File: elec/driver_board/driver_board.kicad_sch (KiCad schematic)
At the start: 0 parts

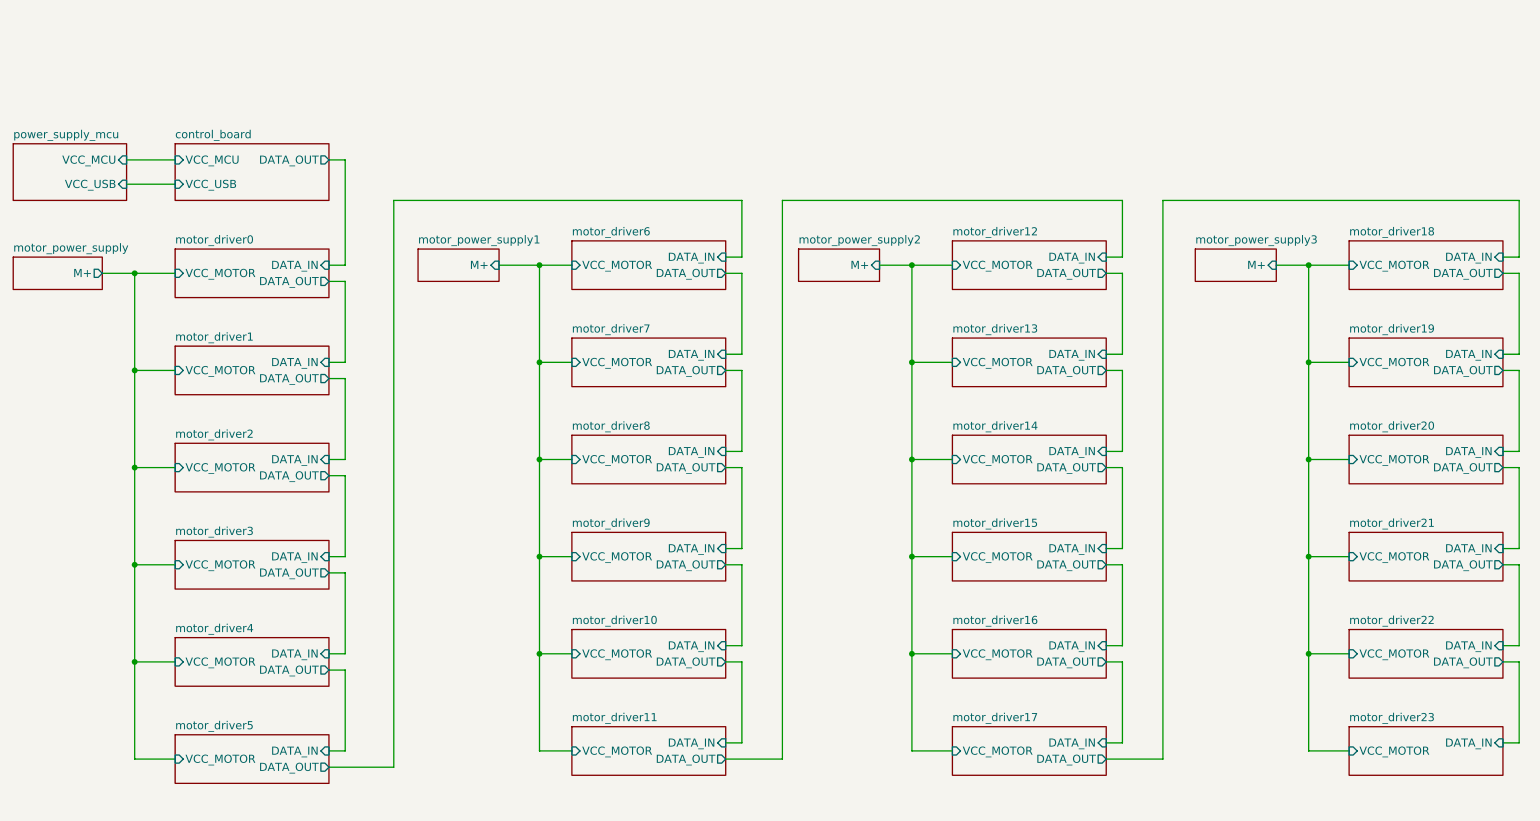
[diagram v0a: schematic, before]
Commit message: [elec] New design with BKA30D-R5
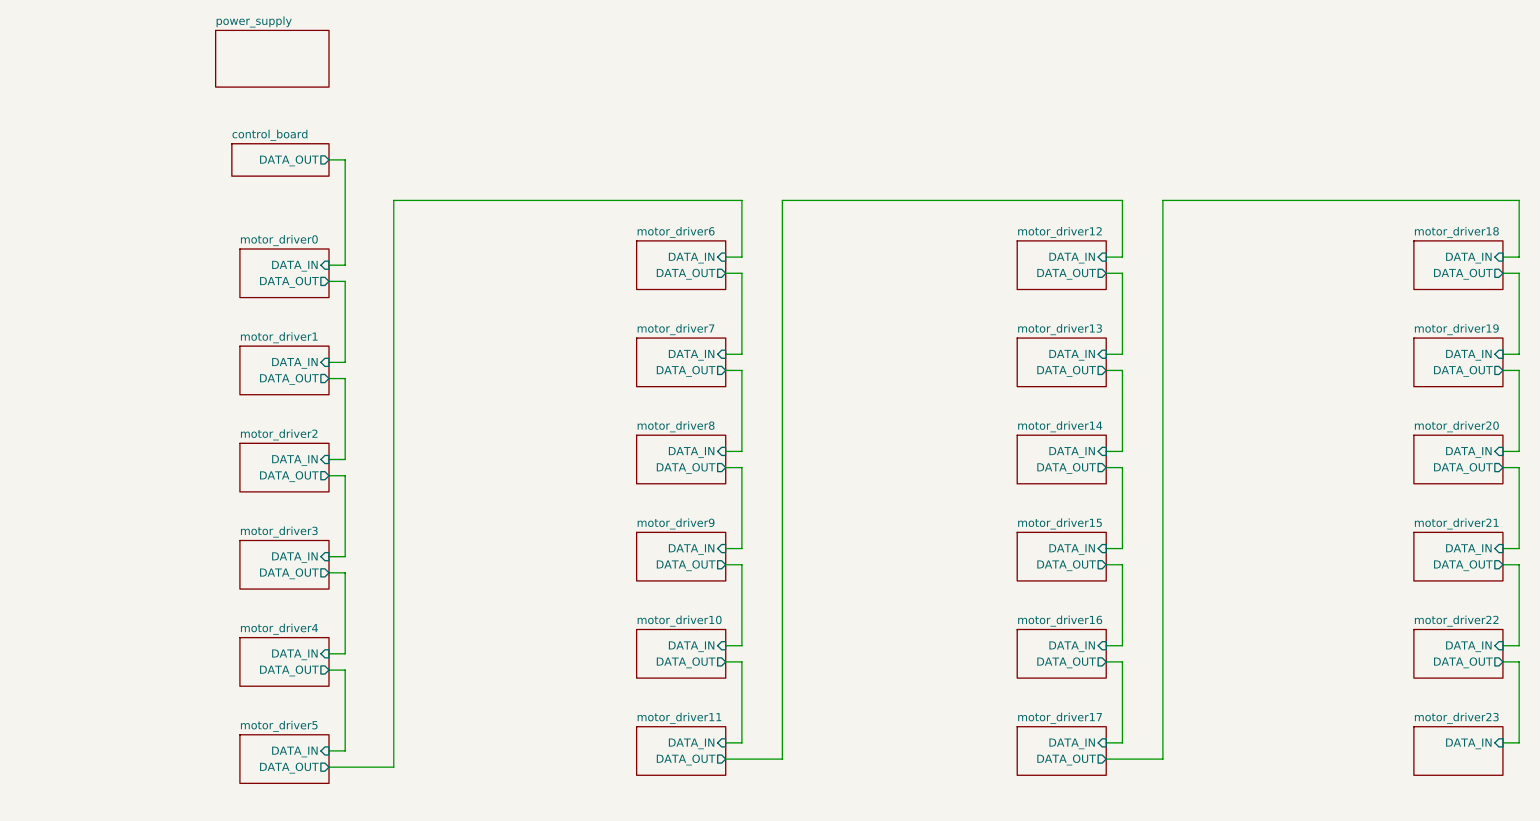
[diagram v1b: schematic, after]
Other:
- sheet power_supply_mcu renamed power_supply
- removed sheet motor_power_supply
- removed sheet motor_power_supply1
- removed sheet motor_power_supply2
- removed sheet motor_power_supply3
- sheet control_board ports: added none; removed VCC_MCU, VCC_USB
- sheet motor_driver0 ports: added none; removed VCC_MOTOR
- sheet motor_driver1 ports: added none; removed VCC_MOTOR
- sheet motor_driver10 ports: added none; removed VCC_MOTOR
- sheet motor_driver11 ports: added none; removed VCC_MOTOR
- sheet motor_driver12 ports: added none; removed VCC_MOTOR
- sheet motor_driver13 ports: added none; removed VCC_MOTOR
- sheet motor_driver14 ports: added none; removed VCC_MOTOR
- sheet motor_driver15 ports: added none; removed VCC_MOTOR
- sheet motor_driver16 ports: added none; removed VCC_MOTOR
- sheet motor_driver17 ports: added none; removed VCC_MOTOR
- sheet motor_driver18 ports: added none; removed VCC_MOTOR
- sheet motor_driver19 ports: added none; removed VCC_MOTOR
- sheet motor_driver2 ports: added none; removed VCC_MOTOR
- sheet motor_driver20 ports: added none; removed VCC_MOTOR
- sheet motor_driver21 ports: added none; removed VCC_MOTOR
- sheet motor_driver22 ports: added none; removed VCC_MOTOR
- sheet motor_driver23 ports: added none; removed VCC_MOTOR
- sheet motor_driver3 ports: added none; removed VCC_MOTOR
- sheet motor_driver4 ports: added none; removed VCC_MOTOR
- sheet motor_driver5 ports: added none; removed VCC_MOTOR
- sheet motor_driver6 ports: added none; removed VCC_MOTOR
- sheet motor_driver7 ports: added none; removed VCC_MOTOR
- sheet motor_driver8 ports: added none; removed VCC_MOTOR
- sheet motor_driver9 ports: added none; removed VCC_MOTOR
- sheet power_supply ports: added none; removed VCC_MCU, VCC_USB

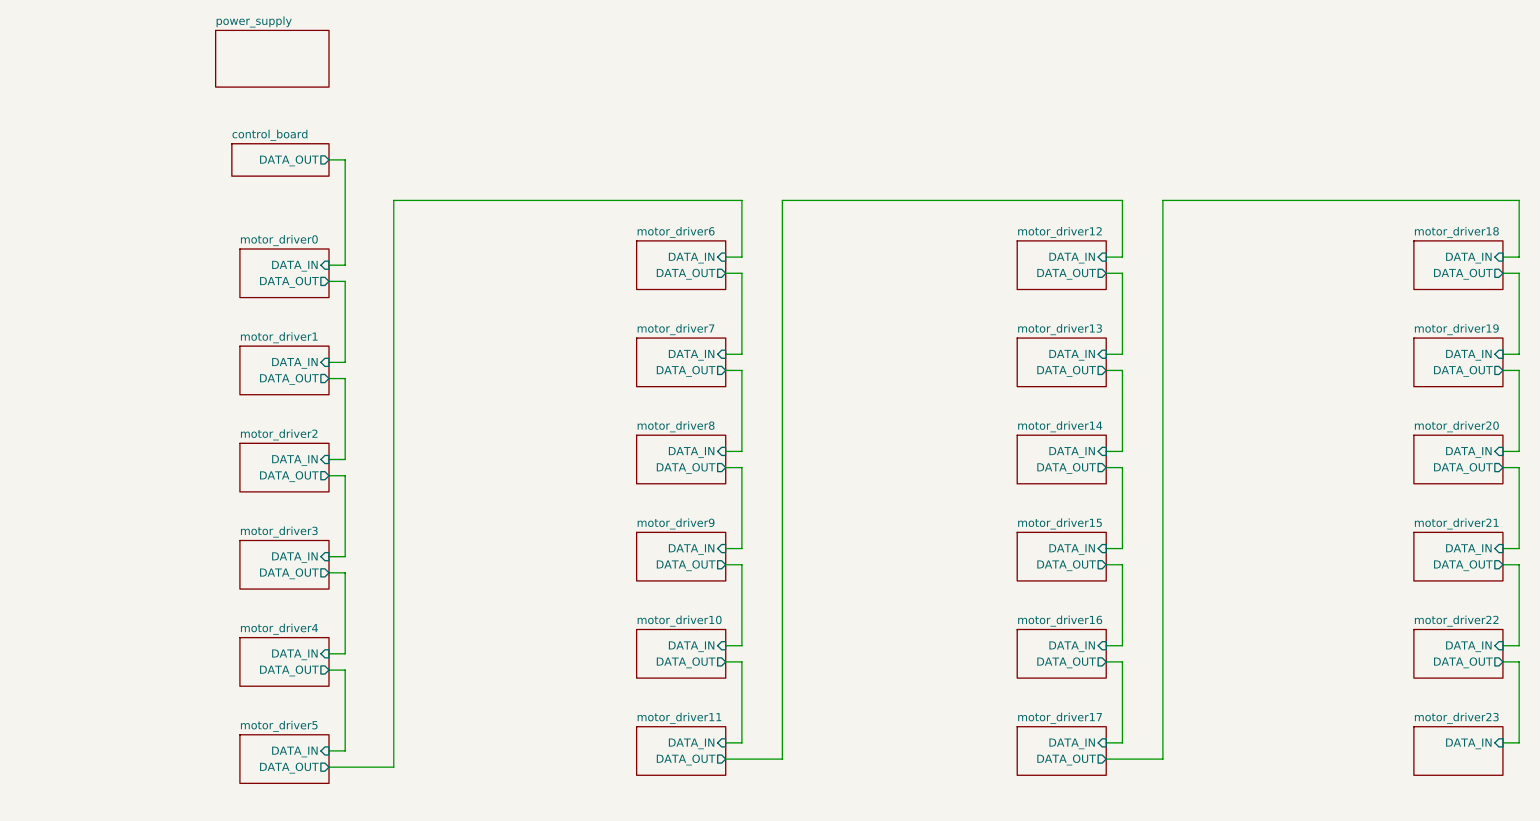
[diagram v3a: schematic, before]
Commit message: Update schematic with VID6606
Use the 'official' driver of VID28-05 motors.
Put back the 74HCT595 bit shift register to link all
motor drivers.
Work in progress.
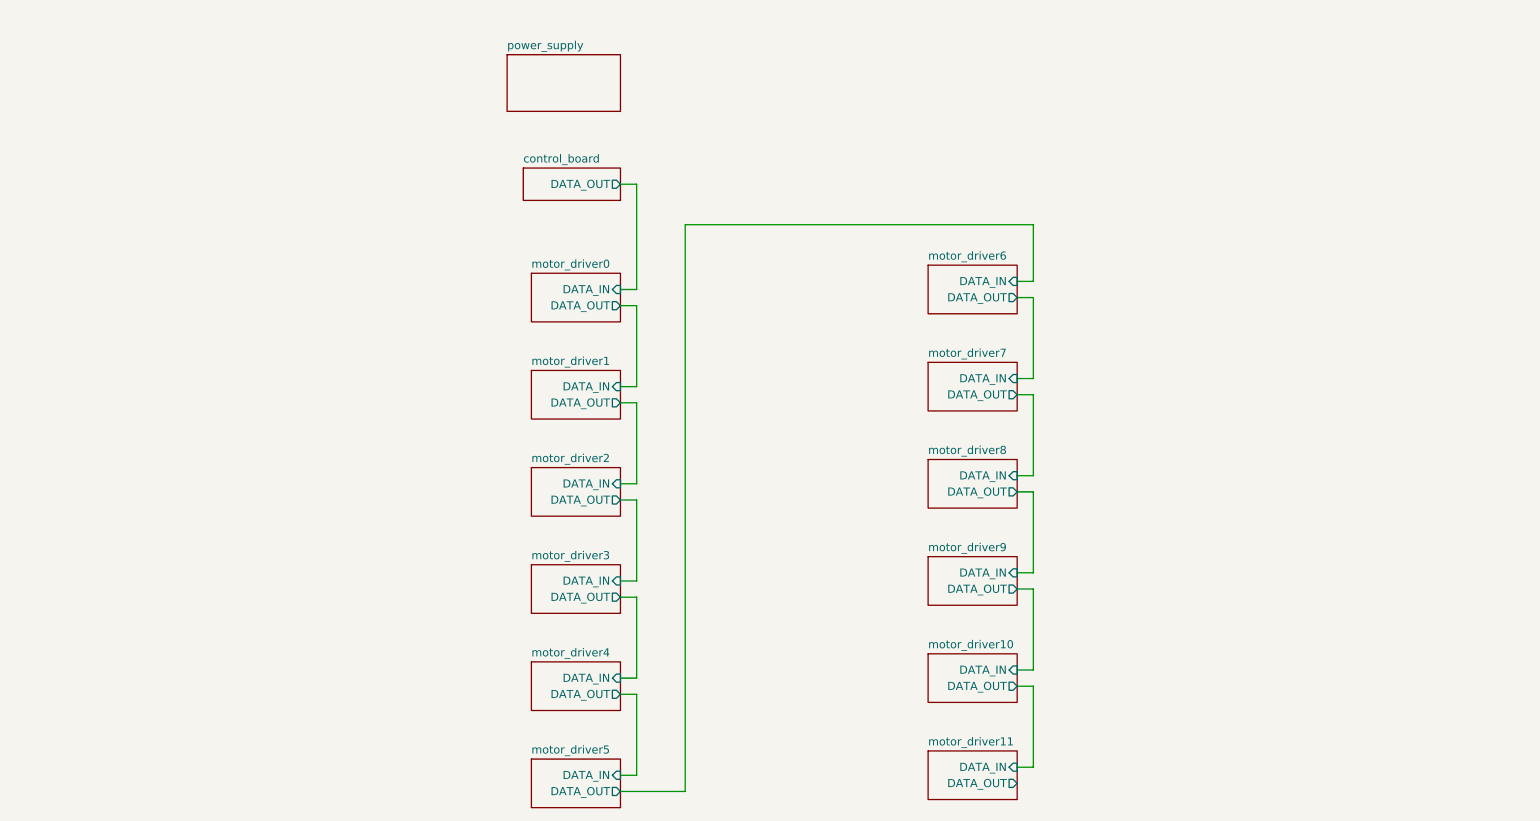
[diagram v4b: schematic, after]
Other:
- removed sheet motor_driver12
- removed sheet motor_driver13
- removed sheet motor_driver14
- removed sheet motor_driver15
- removed sheet motor_driver16
- removed sheet motor_driver17
- removed sheet motor_driver18
- removed sheet motor_driver19
- removed sheet motor_driver20
- removed sheet motor_driver21
- removed sheet motor_driver22
- removed sheet motor_driver23

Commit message: Update silkscreen
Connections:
- no-connect marks 0 -> 1
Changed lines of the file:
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@@
 		(rev "2")
+	)
+	(no_connect
+		(at 180.34 153.67)
 	)
 	(wire

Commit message: Update page number
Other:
- title: (none) -> Clockclock
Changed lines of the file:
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@@
 	(paper "A4")
 	(title_block
-		(date "2025-01-26")
-		(rev "2")
+		(title "Clockclock")
+		(date "2025-02-26")
+		(rev "3")
 	)
 	(no_connect
@@
 			(project "driver_board"
 				(path "/f74582a2-e122-4df8-8bf1-319684e69fbe"
-					(page "5")
+					(page "6")
 				)
 			)
@@
 			(project "driver_board"
 				(path "/f74582a2-e122-4df8-8bf1-319684e69fbe"
-					(page "6")
+					(page "7")
 				)
 			)
@@
 			(project "driver_board"
 				(path "/f74582a2-e122-4df8-8bf1-319684e69fbe"
-					(page "4")
+					(page "5")
 				)
 			)
@@
 			(project "driver_board"
 				(path "/f74582a2-e122-4df8-8bf1-319684e69fbe"
-					(page "0")
+					(page "2")
 				)
 			)
@@
 			(project "driver_board"
 				(path "/f74582a2-e122-4df8-8bf1-319684e69fbe"
-					(page "2")
+					(page "3")
 				)
 			)
@@
 			(project "driver_board"
 				(path "/f74582a2-e122-4df8-8bf1-319684e69fbe"
-					(page "3")
+					(page "4")
 				)
 			)
@@
 			(project "driver_board"
 				(path "/f74582a2-e122-4df8-8bf1-319684e69fbe"
-					(page "7")
+					(page "8")
 				)
 			)
@@
 	(sheet_instances
 		(path "/"
-			(page "1")
-		)
-	)
+			(page "0")
+		)
+	)
